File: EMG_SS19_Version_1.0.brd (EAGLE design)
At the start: 416.5 x 987.7 mm, 212 parts, among them T11 OPA388, T12 OPA388, T21 OPA388, T22 OPA388

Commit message: Bauteile des Digital-Teils auf dem Board platziert
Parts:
- moved JP15 925.2 mm to (97.8, 76.2)
- moved R120 924.1 mm to (120.7, 90.2), turned to 90 degrees
- moved R122 924.1 mm to (133.3, 90.2), turned to 90 degrees
- moved LED_ACT 923.7 mm to (104.1, 88.9), turned to 90 degrees
- moved P5 916.9 mm to (156.2, 83.8), turned to 90 degrees
- moved P6 916.3 mm to (146.1, 96.5), turned to 180 degrees
- moved R121 914.6 mm to (120.7, 82.5), turned to 270 degrees
- moved R123 914.6 mm to (133.3, 82.5), turned to 270 degrees
- moved R117 914.4 mm to (104.1, 82.5), turned to 90 degrees
- moved LED4 897.2 mm to (73.7, 62.2), turned to 270 degrees
- moved BTN_1 895.2 mm to (111.8, 91.4)
- moved BTN_3 894.2 mm to (124.5, 91.4)
- moved R2 891.3 mm to (104.8, 64.5)
- moved R116 889.9 mm to (82.5, 62.2), turned to 90 degrees
- moved LED3 889.3 mm to (87.6, 44.5), turned to 270 degrees
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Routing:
- net VASYS1/2: track 0.00 -> 29.8 mm
- net BTN4: track 0.00 -> 26.0 mm
- net DVCC: track 0.00 -> 24.5 mm
- net N$77: track 0.00 -> 16.9 mm
- net VREF: track 0.00 -> 4.29 mm
- net P6.0: track 0.00 -> 3.89 mm
- net BTN2: track 0.00 -> 3.89 mm
- net BTN1: track 0.00 -> 3.89 mm
- net AUXVCC2: track 0.00 -> 3.81 mm
- net AUXVCC1: track 0.00 -> 3.81 mm
- net AVCC: track 0.00 -> 3.81 mm
- net VCORE: track 0.00 -> 2.04 mm
- net XOUT: track 0.00 -> 0.71 mm
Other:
- board size 416.5 x 987.7 mm -> 160 x 100 mm

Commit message: next version of digital part implementation
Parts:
- moved DGND2 51.0 mm to (111.1, 66.4)
- moved DGND1 32.3 mm to (111.5, 25.0)
- moved C29 24.7 mm to (109.1, 47.9), turned to 90 degrees
- moved C31 20.7 mm to (106.8, 47.9), turned to 90 degrees
- moved C25 19.1 mm to (105.8, 34.0), turned to 180 degrees
- moved C24 14.2 mm to (105.8, 37.8), turned to 180 degrees
- moved R1 11.2 mm to (92.6, 30.2)
- moved C27 10.2 mm to (107.5, 42.4)
- moved C26 4.65 mm to (104.6, 42.5)
- moved R2 4.38 mm to (100.5, 65.2), turned to 180 degrees
- moved C28 3.81 mm to (114.0, 57.3), turned to 270 degrees
- moved C32 3.81 mm to (110.2, 57.3), turned to 270 degrees
- moved C33 0.76 mm to (118.9, 44.8)
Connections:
- removed net P6.0: BTN_3.2, P6.1, R122.2, U$1.77
- new net N$93: P6.1, U$1.77
- new net N$95: U$1.93
- net ACT_LED: now also U$1.83; no longer U$1.93
- net BTN1: now also U$1.86; no longer U$1.91
- net BTN2: now also U$1.85; no longer U$1.92
- net BTN3: now also BTN_3.2, R122.2; no longer U$1.83
- net LED1: now also U$1.92; no longer U$1.85
- net LED2: now also U$1.91; no longer U$1.86
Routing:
- net ACT_LED: track 0.00 -> 69.4 mm
- net BTN1: track 3.89 -> 52.2 mm
- net N$78: track 0.00 -> 47.1 mm
- net N$90: track 0.00 -> 46.9 mm
- net N$79: track 0.00 -> 46.2 mm
- net N$56: track 0.00 -> 45.8 mm
- net N$89: track 0.00 -> 44.9 mm
- net N$93: track 0.00 -> 44.1 mm
- net N$92: track 0.00 -> 43.2 mm
- net N$63: track 0.00 -> 43.1 mm
- net N$88: track 0.00 -> 43.0 mm
- net P6.2: track 0.00 -> 42.4 mm
- net P6.5: track 0.00 -> 41.7 mm
- net P6.3: track 0.00 -> 41.5 mm
- net N$87: track 0.00 -> 41.1 mm
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- added copper zone on layer 1, net DGND

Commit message: first version of analog & digital part completed --> ready for review
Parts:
- moved JP16 53.4 mm to (101.5, 72.5), turned to 0 degrees
- moved R2 40.0 mm to (100.5, 25.2)
- moved DGND2 29.9 mm to (107.2, 96.0)
- moved R101 23.1 mm to (107.7, 19.7), turned to 0 degrees
- moved C110 23.1 mm to (107.8, 17.0), turned to 0 degrees
- moved R1 17.2 mm to (104.3, 42.7), turned to 90 degrees
- moved RESET 14.4 mm to (112.8, 19.7), turned to 0 degrees
- moved C29 11.1 mm to (120.1, 48.8)
- moved C31 11.1 mm to (117.9, 48.8)
- moved JP15 9.91 mm to (106.9, 72.4)
- moved XT1 8.67 mm to (120.3, 38.5), turned to 90 degrees
- moved C25 7.50 mm to (112.0, 38.2)
- moved DGND1 7.47 mm to (105.9, 30.0)
- moved C24 6.82 mm to (112.0, 40.6)
- moved C101 5.17 mm to (125.0, 34.2)
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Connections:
- removed net +3V: C+3.+, JP7.8
- removed net N$95: U$1.93
- net ACT_LED: now also U$1.87; no longer U$1.83
- net AGND: now also U$1.6; no longer U$1.13
- net BTN3: now also U$1.83
- net DGND: now also U$1.12, U$1.13; no longer U$1.5, U$1.6
- net DVCC: now also C+3.+, JP7.8
- net LED1: now also U$1.93; no longer U$1.92
- net LED3: now also U$1.88; no longer U$1.87
- net LED4: now also U$1.89; no longer U$1.88
- net LED5: now also U$1.90; no longer U$1.89
- net LED6: now also U$1.92; no longer U$1.90
- net SD_IN_2P: now also U$1.5; no longer U$1.12
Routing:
- net DVCC: track 24.5 -> 358.9 mm, vias 0 -> 6
- net +3V: track 133.1 -> 0.00 mm, vias 2 -> 0
- net LS_TO_ADC2: track 103.4 -> 208.1 mm, vias 0 -> 2
- net TDO: track 0.00 -> 80.1 mm, vias 0 -> 2
- net RESET: track 19.2 -> 91.4 mm, vias 0 -> 2
- net TEST/SBWTCK: track 0.00 -> 70.7 mm, vias 0 -> 2
- net TDI: track 0.00 -> 70.4 mm, vias 0 -> 2
- net LED5: track 0.00 -> 69.8 mm, vias 0 -> 2
- net LED6: track 0.00 -> 69.0 mm, vias 0 -> 2
- net TMS: track 0.00 -> 67.2 mm, vias 0 -> 2
- net LED4: track 0.00 -> 63.1 mm, vias 0 -> 2
- net TCK: track 0.00 -> 57.6 mm, vias 0 -> 2
- net N$82: track 0.00 -> 57.1 mm
- net RTCCLK: track 0.00 -> 56.0 mm, vias 0 -> 2
- net N$81: track 0.00 -> 53.0 mm
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
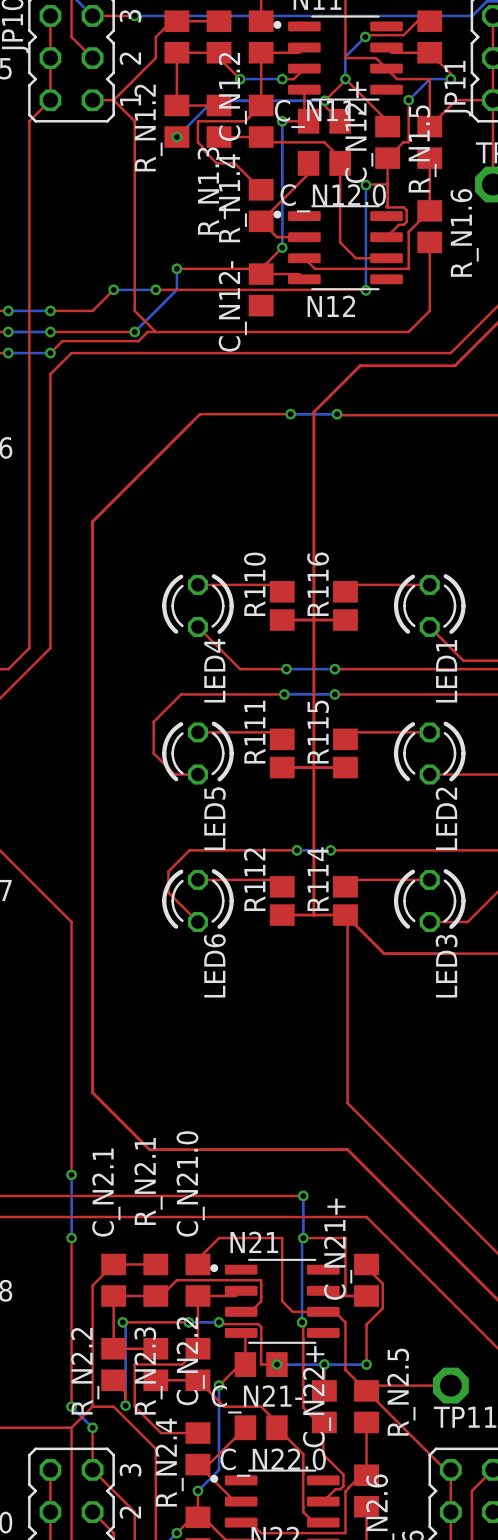
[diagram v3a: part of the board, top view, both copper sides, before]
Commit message: modified version of analog & digital part complete
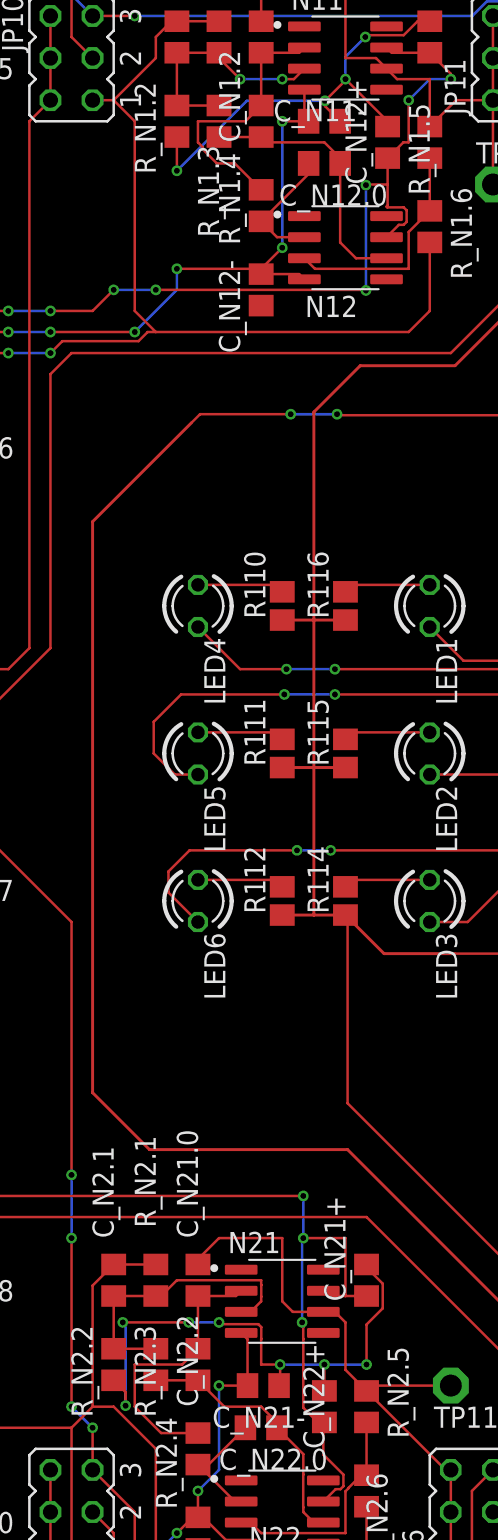
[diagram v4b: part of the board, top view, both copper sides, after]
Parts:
- moved C_N21- 1.28 mm to (77.6, 15.2)
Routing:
- net AGND: track 61.8 -> 66.1 mm
- net -1.5V: track 265.8 -> 266.7 mm
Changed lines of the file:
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@@
 <attribute name="VALUE" x="86.36" y="20.32" size="1.27" layer="27" rot="R90"/>
 </element>
-<element name="C_N21-" library="rcl" library_urn="urn:adsk.eagle:library:334" package="C0805" package3d_urn="urn:adsk.eagle:package:23617/2" value="100n" x="77.47" y="16.51" smashed="yes" rot="R180">
-<attribute name="NAME" x="80.01" y="15.24" size="1.27" layer="25" rot="R180"/>
-<attribute name="SPICEPREFIX" value="C" x="77.47" y="67.31" size="1.778" layer="27" rot="R180" display="off"/>
-<attribute name="VALUE" x="78.74" y="19.05" size="1.27" layer="27" rot="R180"/>
+<element name="C_N21-" library="rcl" library_urn="urn:adsk.eagle:library:334" package="C0805" package3d_urn="urn:adsk.eagle:package:23617/2" value="100n" x="77.597" y="15.24" smashed="yes" rot="R180">
+<attribute name="NAME" x="80.137" y="13.97" size="1.27" layer="25" rot="R180"/>
+<attribute name="SPICEPREFIX" value="C" x="77.597" y="66.04" size="1.778" layer="27" rot="R180" display="off"/>
+<attribute name="VALUE" x="78.867" y="17.78" size="1.27" layer="27" rot="R180"/>
 </element>
 <element name="C_N22+" library="rcl" library_urn="urn:adsk.eagle:library:334" package="C0805" package3d_urn="urn:adsk.eagle:package:23617/2" value="100n" x="81.28" y="13.97" smashed="yes" rot="R90">
@@
 <wire x1="81.28" y1="14.92" x2="81.28" y2="16.51" width="0.1524" layer="1"/>
 <via x="81.28" y="16.51" extent="1-16" drill="0.35"/>
-<wire x1="81.28" y1="16.51" x2="78.42" y2="16.51" width="0.1524" layer="16"/>
-<via x="78.42" y="16.51" extent="1-16" drill="0.35"/>
+<wire x1="81.28" y1="16.51" x2="78.613" y2="16.51" width="0.1524" layer="16"/>
+<wire x1="78.613" y1="16.51" x2="78.42" y2="16.51" width="0.1524" layer="16"/>
 <wire x1="68.58" y1="15.56" x2="69.2988" y2="14.8412" width="0.1524" layer="1"/>
 <wire x1="69.2988" y1="14.8412" x2="69.2988" y2="14.03071875" width="0.1524" layer="1"/>
@@
 <wire x1="73.1088" y1="19.05" x2="74.93" y2="19.05" width="0.1524" layer="16"/>
 <via x="74.93" y="19.05" extent="1-16" drill="0.35"/>
-<wire x1="77.47" y1="16.51" x2="78.42" y2="16.51" width="0.1524" layer="1"/>
 <wire x1="77.2997625" y1="18.9412" x2="77.4762" y2="18.7647625" width="0.1524" layer="1"/>
 <wire x1="77.4762" y1="18.7647625" x2="77.4762" y2="18.0652375" width="0.1524" layer="1"/>
@@
 <wire x1="77.4762" y1="18.0652375" x2="77.47" y2="18.0590375" width="0.1524" layer="1"/>
 <wire x1="77.47" y1="18.0590375" x2="77.47" y2="16.51" width="0.1524" layer="1"/>
-<via x="72.39" y="90.49" extent="1-16" drill="0.35"/>
-<wire x1="72.39" y1="90.49" x2="74.573590625" y2="92.673590625" width="0.1524" layer="16"/>
-<wire x1="74.573590625" y1="92.673590625" x2="81.316409375" y2="92.673590625" width="0.1524" layer="16"/>
+<via x="72.39" y="88.458" extent="1-16" drill="0.35"/>
+<wire x1="72.39" y1="88.458" x2="76.605590625" y2="92.673590625" width="0.1524" layer="16"/>
+<wire x1="76.605590625" y1="92.673590625" x2="81.316409375" y2="92.673590625" width="0.1524" layer="16"/>
 <via x="81.316409375" y="92.673590625" extent="1-16" drill="0.35"/>
 <wire x1="81.316409375" y1="92.673590625" x2="81.316409375" y2="92.353590625" width="0.1524" layer="1"/>
@@
 <wire x1="123.572" y1="54.3" x2="123.501" y2="54.229" width="0.1524" layer="1"/>
 <wire x1="123.501" y1="54.229" x2="121.031" y2="54.229" width="0.1524" layer="1"/>
+<via x="78.613" y="16.51" extent="1-16" drill="0.35"/>
+<wire x1="78.613" y1="16.51" x2="78.613" y2="15.306" width="0.1524" layer="1"/>
+<wire x1="78.613" y1="15.306" x2="78.547" y2="15.24" width="0.1524" layer="1"/>
+<wire x1="77.47" y1="16.51" x2="78.613" y2="16.51" width="0.1524" layer="1"/>
+<wire x1="72.39" y1="90.49" x2="72.39" y2="88.458" width="0.1524" layer="1"/>
 <wire x1="123.572" y1="54.3" x2="123.533" y2="56.261" width="0" layer="19" extent="1-1"/>
 <wire x1="123.572" y1="52.3" x2="123.501" y2="54.229" width="0" layer="19" extent="1-1"/>
@@
 <wire x1="41.91" y1="90.49" x2="46.99" y2="90.49" width="0" layer="19" extent="1-1"/>
 <wire x1="57.15" y1="97.47" x2="57.15" y2="86.04" width="0" layer="19" extent="1-1"/>
-<wire x1="72.39" y1="90.49" x2="57.15" y2="86.04" width="0" layer="19" extent="1-1"/>
-<wire x1="77.47" y1="80.33" x2="72.39" y2="90.49" width="0" layer="19" extent="1-1"/>
+<wire x1="72.39" y1="88.458" x2="57.15" y2="86.04" width="0" layer="19" extent="1-16"/>
+<wire x1="77.47" y1="80.33" x2="72.39" y2="88.458" width="0" layer="19" extent="1-16"/>
 <wire x1="25.7556" y1="43.434" x2="41.91" y2="40.96" width="0" layer="19" extent="1-1"/>
 <wire x1="19.05" y1="35.08" x2="25.7556" y2="43.434" width="0" layer="19" extent="1-1"/>
@@
 <wire x1="46.99" y1="4.76" x2="47.945" y2="5.715" width="0.1524" layer="1"/>
 <wire x1="47.945" y1="5.715" x2="49.595" y2="5.715" width="0.1524" layer="1"/>
-<wire x1="76.52" y1="16.51" x2="76.52" y2="18.16" width="0.1524" layer="1"/>
-<wire x1="76.52" y1="18.16" x2="76.265" y2="18.415" width="0.1524" layer="1"/>
+<wire x1="76.647" y1="15.24" x2="76.647" y2="18.033" width="0.1524" layer="1"/>
+<wire x1="76.647" y1="18.033" x2="76.265" y2="18.415" width="0.1524" layer="1"/>
 <wire x1="73.66" y1="7.3" x2="73.98" y2="7.3" width="0.1524" layer="1"/>
 <wire x1="75.565" y1="5.715" x2="76.265" y2="5.715" width="0.1524" layer="1"/>
@@
 <wire x1="74.93" y1="10.16" x2="74.93" y2="15.24" width="0.1524" layer="16"/>
 <via x="74.93" y="15.24" extent="1-16" drill="0.35"/>
-<wire x1="74.93" y1="15.24" x2="76.2" y2="16.51" width="0.1524" layer="1"/>
-<wire x1="76.2" y1="16.51" x2="76.52" y2="16.51" width="0.1524" layer="1"/>
+<wire x1="74.93" y1="15.24" x2="76.647" y2="15.24" width="0.1524" layer="1"/>
 <via x="67.31" y="3.81" extent="1-16" drill="0.35"/>
 <wire x1="58.96084375" y1="3.7743" x2="58.99654375" y2="3.81" width="0.1524" layer="1"/>
